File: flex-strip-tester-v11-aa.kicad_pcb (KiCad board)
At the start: 2 copper layers, 68.8 x 11.1 mm, 12 parts, among them J2 Conn_01x01_Female

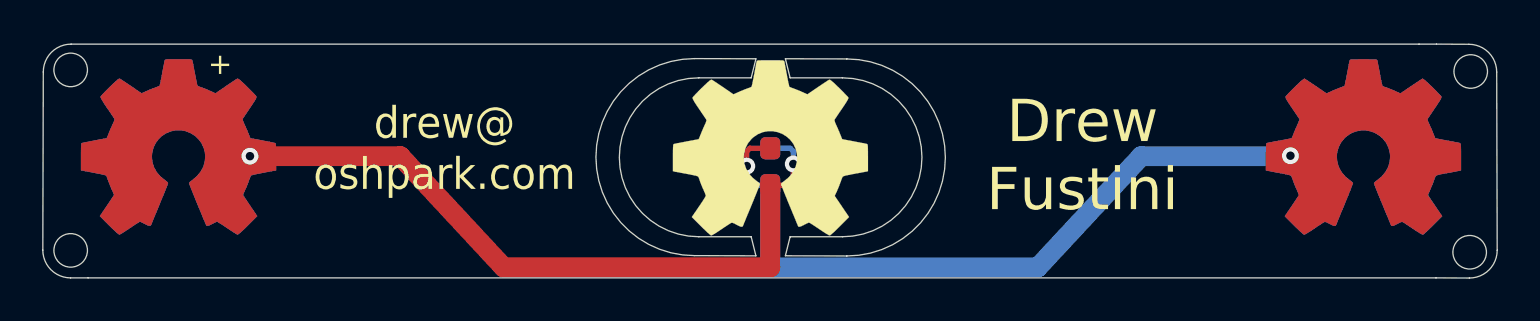
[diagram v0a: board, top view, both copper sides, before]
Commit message: add new version v11 for AA/AAA battery
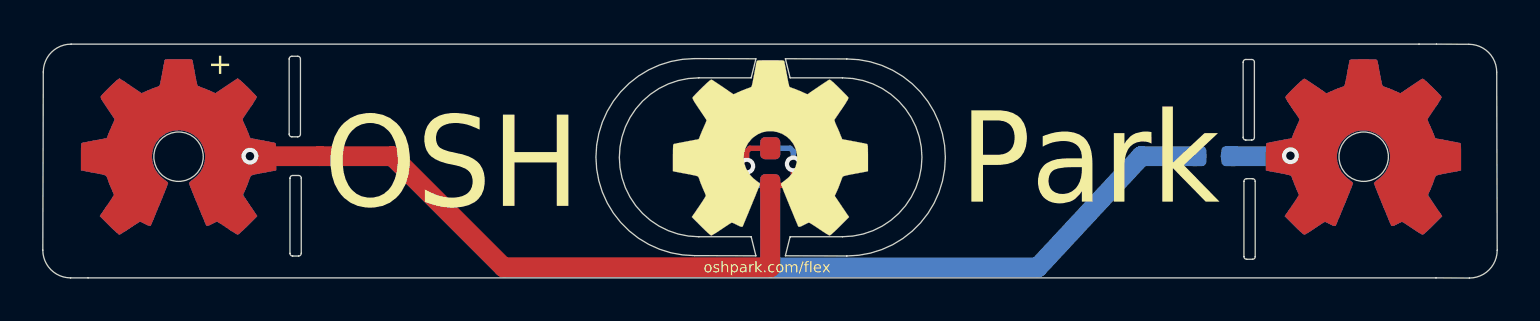
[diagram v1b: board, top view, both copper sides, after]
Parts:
- added REF**: R_0603, Resistor_SMD:R_0603_1608Metric, B.Cu at (174.2, 95.5)
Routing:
- net +3V3: track 34.7 -> 30.2 mm, vias 2 -> 1
- net GND: track 34.6 -> 37.6 mm, vias 2 -> 3
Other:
- outline, holes or cut-outs redrawn
- board text added: "OSH"
- board text added: "Park"
- board text added: "oshpark.com/flex"
- board text removed: "Drew Fustini"
- board text removed: "drew@ oshpark.com"
